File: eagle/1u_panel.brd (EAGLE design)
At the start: 83 x 100 mm, 65 parts, among them J1 1.27MM-SWD-CONNECTOR, U1 SPV1040, U5 P-CHANNELFET, U6 ON-N-CHANNEL-FET, U7 DIODE-INC-NPNSOT23HOLE

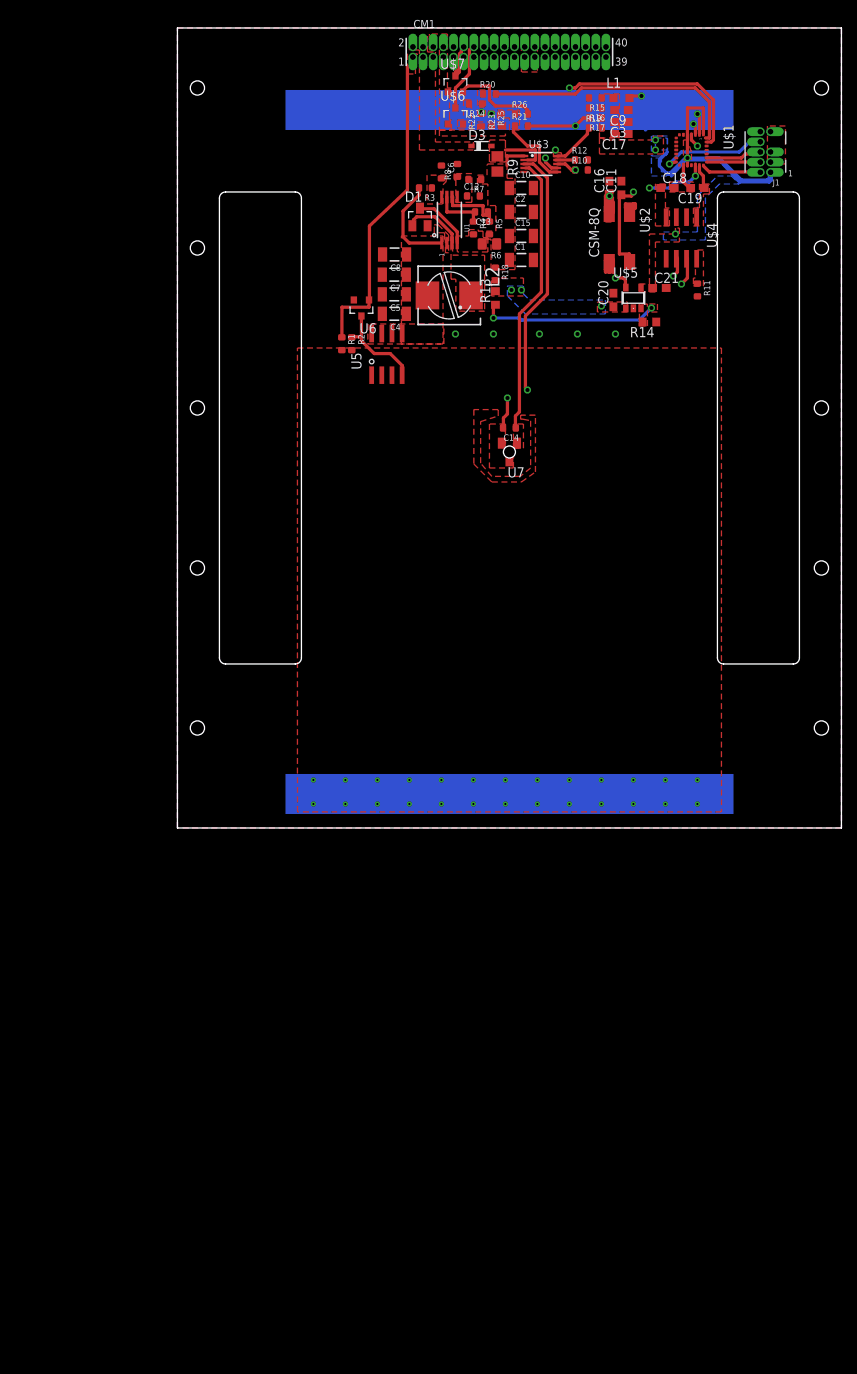
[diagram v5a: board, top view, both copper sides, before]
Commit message: OreSat rev0.5 structure changes with Calvin.
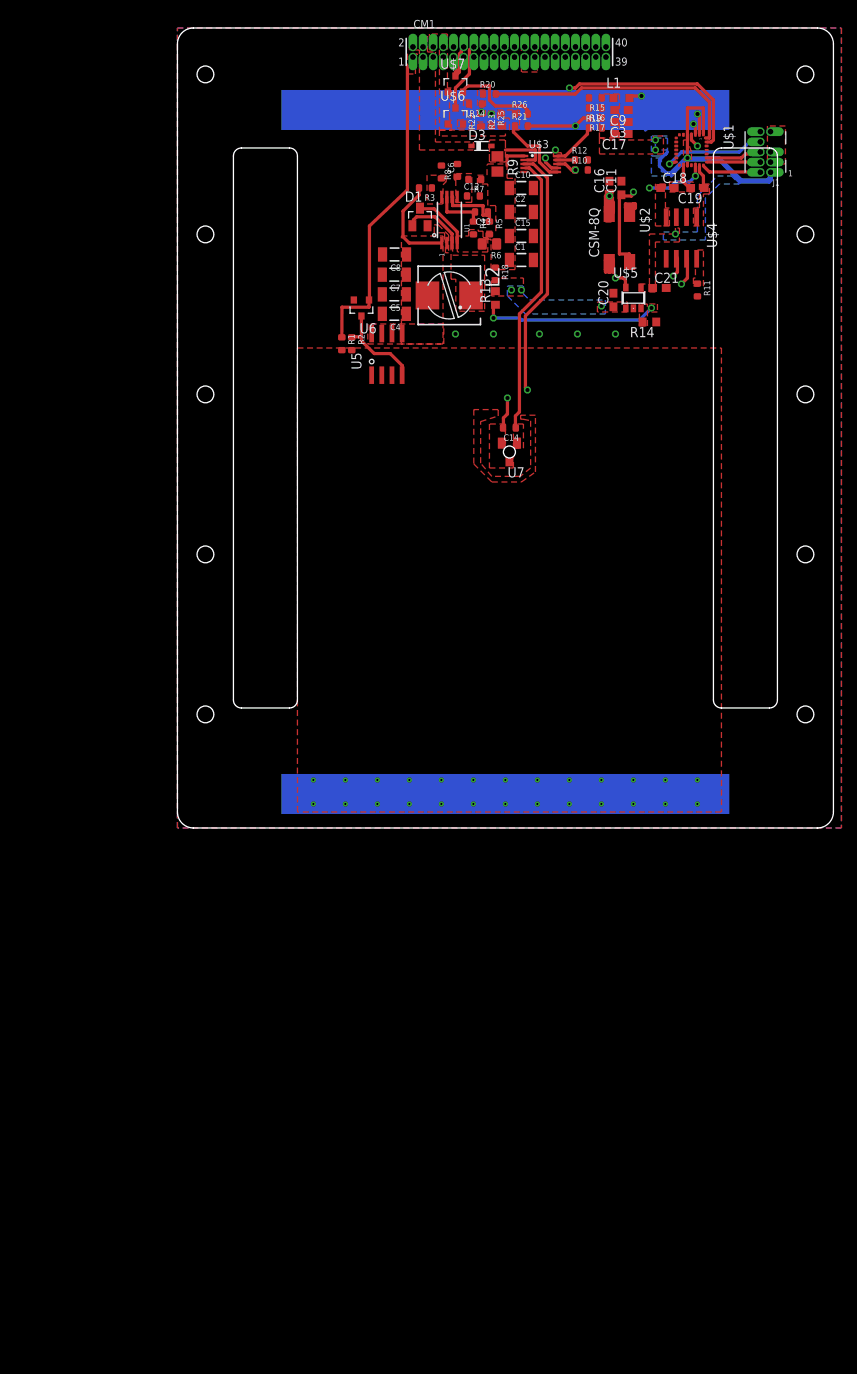
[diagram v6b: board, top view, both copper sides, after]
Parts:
- moved D2 0.50 mm to (41.0, 47.0)
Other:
- board size 83 x 100 mm -> 82 x 100 mm
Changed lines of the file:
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@@
 <?xml version="1.0" encoding="utf-8"?>
 <!DOCTYPE eagle SYSTEM "eagle.dtd">
-<eagle version="7.5.0">
+<eagle version="7.7.0">
 <drawing>
 <settings>
@@
 <layer number="23" name="tOrigins" color="15" fill="1" visible="yes" active="yes"/>
 <layer number="24" name="bOrigins" color="15" fill="1" visible="yes" active="yes"/>
-<layer number="25" name="tNames" color="7" fill="1" visible="yes" active="yes"/>
-<layer number="26" name="bNames" color="7" fill="1" visible="yes" active="yes"/>
-<layer number="27" name="tValues" color="7" fill="1" visible="yes" active="yes"/>
-<layer number="28" name="bValues" color="7" fill="1" visible="yes" active="yes"/>
+<layer number="25" name="tNames" color="7" fill="1" visible="no" active="yes"/>
+<layer number="26" name="bNames" color="7" fill="1" visible="no" active="yes"/>
+<layer number="27" name="tValues" color="7" fill="1" visible="no" active="yes"/>
+<layer number="28" name="bValues" color="7" fill="1" visible="no" active="yes"/>
 <layer number="29" name="tStop" color="7" fill="3" visible="yes" active="yes"/>
 <layer number="30" name="bStop" color="7" fill="6" visible="yes" active="yes"/>
-<layer number="31" name="tCream" color="7" fill="4" visible="yes" active="yes"/>
-<layer number="32" name="bCream" color="7" fill="5" visible="yes" active="yes"/>
-<layer number="33" name="tFinish" color="6" fill="3" visible="yes" active="yes"/>
-<layer number="34" name="bFinish" color="6" fill="6" visible="yes" active="yes"/>
-<layer number="35" name="tGlue" color="7" fill="4" visible="yes" active="yes"/>
-<layer number="36" name="bGlue" color="7" fill="5" visible="yes" active="yes"/>
-<layer number="37" name="tTest" color="7" fill="1" visible="yes" active="yes"/>
-<layer number="38" name="bTest" color="7" fill="1" visible="yes" active="yes"/>
-<layer number="39" name="tKeepout" color="4" fill="11" visible="yes" active="yes"/>
-<layer number="40" name="bKeepout" color="1" fill="11" visible="yes" active="yes"/>
-<layer number="41" name="tRestrict" color="4" fill="10" visible="yes" active="yes"/>
-<layer number="42" name="bRestrict" color="1" fill="10" visible="yes" active="yes"/>
-<layer number="43" name="vRestrict" color="2" fill="10" visible="yes" active="yes"/>
-<layer number="44" name="Drills" color="7" fill="1" visible="yes" active="yes"/>
-<layer number="45" name="Holes" color="7" fill="1" visible="yes" active="yes"/>
+<layer number="31" name="tCream" color="7" fill="4" visible="no" active="yes"/>
+<layer number="32" name="bCream" color="7" fill="5" visible="no" active="yes"/>
+<layer number="33" name="tFinish" color="6" fill="3" visible="no" active="yes"/>
+<layer number="34" name="bFinish" color="6" fill="6" visible="no" active="yes"/>
+<layer number="35" name="tGlue" color="7" fill="4" visible="no" active="yes"/>
+<layer number="36" name="bGlue" color="7" fill="5" visible="no" active="yes"/>
+<layer number="37" name="tTest" color="7" fill="1" visible="no" active="yes"/>
+<layer number="38" name="bTest" color="7" fill="1" visible="no" active="yes"/>
+<layer number="39" name="tKeepout" color="4" fill="11" visible="no" active="yes"/>
+<layer number="40" name="bKeepout" color="1" fill="11" visible="no" active="yes"/>
+<layer number="41" name="tRestrict" color="4" fill="10" visible="no" active="yes"/>
+<layer number="42" name="bRestrict" color="1" fill="10" visible="no" active="yes"/>
+<layer number="43" name="vRestrict" color="2" fill="10" visible="no" active="yes"/>
+<layer number="44" name="Drills" color="7" fill="1" visible="no" active="yes"/>
+<layer number="45" name="Holes" color="7" fill="1" visible="no" active="yes"/>
 <layer number="46" name="Milling" color="3" fill="1" visible="yes" active="yes"/>
-<layer number="47" name="Measures" color="7" fill="1" visible="yes" active="yes"/>
+<layer number="47" name="Measures" color="7" fill="1" visible="no" active="yes"/>
 <layer number="48" name="Document" color="7" fill="1" visible="yes" active="yes"/>
-<layer number="49" name="Reference" color="7" fill="1" visible="yes" active="yes"/>
+<layer number="49" name="Reference" color="7" fill="1" visible="no" active="yes"/>
 <layer number="51" name="tDocu" color="7" fill="1" visible="yes" active="yes"/>
 <layer number="52" name="bDocu" color="7" fill="1" visible="yes" active="yes"/>
@@
 <board>
 <plain>
-<wire x1="0" y1="0" x2="83" y2="0" width="0" layer="20"/>
-<wire x1="83" y1="0" x2="83" y2="100" width="0" layer="20"/>
-<wire x1="83" y1="100" x2="0" y2="100" width="0" layer="20"/>
-<wire x1="0" y1="100" x2="0" y2="0" width="0" layer="20"/>
-<hole x="2.5" y="12.5" drill="1.78"/>
-<hole x="2.5" y="32.5" drill="1.78"/>
-<hole x="2.5" y="52.5" drill="1.78"/>
-<hole x="2.5" y="72.5" drill="1.78"/>
-<hole x="2.5" y="92.5" drill="1.78"/>
-<hole x="80.5" y="12.5" drill="1.78"/>
-<hole x="80.5" y="32.5" drill="1.78"/>
-<hole x="80.5" y="52.5" drill="1.78"/>
-<hole x="80.5" y="72.5" drill="1.78"/>
-<hole x="80.5" y="92.5" drill="1.78"/>
-<wire x1="14.732" y1="20.5" x2="6.018" y2="20.5" width="0.1" layer="20"/>
-<wire x1="6.018" y1="20.5" x2="5.25" y2="21.268" width="0.1" layer="20" curve="-90"/>
-<wire x1="5.25" y1="21.268" x2="5.25" y2="78.732" width="0.1" layer="20"/>
-<wire x1="5.25" y1="78.732" x2="6.018" y2="79.5" width="0.1" layer="20" curve="-90"/>
-<wire x1="6.018" y1="79.5" x2="14.732" y2="79.5" width="0.1" layer="20"/>
-<wire x1="14.732" y1="79.5" x2="15.5" y2="78.732" width="0.1" layer="20" curve="-90"/>
-<wire x1="15.5" y1="78.732" x2="15.5" y2="21.268" width="0.1" layer="20"/>
-<wire x1="15.5" y1="21.268" x2="14.732" y2="20.5" width="0.1" layer="20" curve="-90"/>
-<wire x1="68.268" y1="20.5" x2="76.982" y2="20.5" width="0.1" layer="20"/>
-<wire x1="76.982" y1="20.5" x2="77.75" y2="21.268" width="0.1" layer="20" curve="90"/>
-<wire x1="77.75" y1="21.268" x2="77.75" y2="78.732" width="0.1" layer="20"/>
-<wire x1="77.75" y1="78.732" x2="76.982" y2="79.5" width="0.1" layer="20" curve="90"/>
-<wire x1="76.982" y1="79.5" x2="68.268" y2="79.5" width="0.1" layer="20"/>
-<wire x1="68.268" y1="79.5" x2="67.5" y2="78.732" width="0.1" layer="20" curve="90"/>
-<wire x1="67.5" y1="78.732" x2="67.5" y2="21.268" width="0.1" layer="20"/>
-<wire x1="67.5" y1="21.268" x2="68.268" y2="20.5" width="0.1" layer="20" curve="90"/>
+<wire x1="80" y1="100" x2="2" y2="100" width="0" layer="20"/>
+<wire x1="2" y1="100" x2="0" y2="98" width="0" layer="20" curve="90"/>
+<wire x1="0" y1="98" x2="0" y2="2" width="0" layer="20"/>
+<wire x1="0" y1="2" x2="2" y2="0" width="0" layer="20" curve="90"/>
+<wire x1="2" y1="0" x2="80" y2="0" width="0" layer="20"/>
+<wire x1="80" y1="0" x2="82" y2="2" width="0" layer="20" curve="90"/>
+<wire x1="82" y1="2" x2="82" y2="98" width="0" layer="20"/>
+<wire x1="82" y1="98" x2="80" y2="100" width="0" layer="20" curve="90"/>
+<hole x="3.5" y="14.2" drill="2.1"/>
+<hole x="3.5" y="34.2" drill="2.1"/>
+<hole x="3.5" y="54.2" drill="2.1"/>
+<hole x="3.5" y="74.2" drill="2.1"/>
+<hole x="3.5" y="94.2" drill="2.1"/>
+<hole x="78.5" y="14.2" drill="2.1"/>
+<hole x="78.5" y="34.2" drill="2.1"/>
+<hole x="78.5" y="54.2" drill="2.1"/>
+<hole x="78.5" y="74.2" drill="2.1"/>
+<hole x="78.5" y="94.2" drill="2.1"/>
+<wire x1="15" y1="84" x2="15" y2="16" width="0.1" layer="20"/>
+<wire x1="15" y1="16" x2="14" y2="15" width="0.1" layer="20" curve="-90"/>
+<wire x1="14" y1="15" x2="8" y2="15" width="0.1" layer="20"/>
+<wire x1="8" y1="15" x2="7" y2="16" width="0.1" layer="20" curve="-90"/>
+<wire x1="7" y1="16" x2="7" y2="84" width="0.1" layer="20"/>
+<wire x1="7" y1="84" x2="8" y2="85" width="0.1" layer="20" curve="-90"/>
+<wire x1="8" y1="85" x2="14" y2="85" width="0.1" layer="20"/>
+<wire x1="14" y1="85" x2="15" y2="84" width="0.1" layer="20" curve="-90"/>
+<wire x1="67" y1="16" x2="67" y2="84" width="0.1" layer="20"/>
+<wire x1="67" y1="84" x2="68" y2="85" width="0.1" layer="20" curve="-90"/>
+<wire x1="68" y1="85" x2="74" y2="85" width="0.1" layer="20"/>
+<wire x1="67" y1="16" x2="68" y2="15" width="0.1" layer="20" curve="90"/>
+<wire x1="68" y1="15" x2="74" y2="15" width="0.1" layer="20"/>
+<wire x1="74" y1="15" x2="75" y2="16" width="0.1" layer="20" curve="90"/>
+<wire x1="74" y1="85" x2="75" y2="84" width="0.1" layer="20" curve="-90"/>
+<wire x1="75" y1="84" x2="75" y2="16" width="0.1" layer="20"/>
 </plain>
 <attributes>
@@
 <element name="R9" library="rcl" package="R0805" value="" x="40" y="83" rot="R270"/>
 <element name="C14" library="rcl_custom" package=".0603-B-NOSILK" value="20u" x="41.5" y="50" rot="R180"/>
-<element name="D2" library="alta-cell" package="ALTA-FIVE-CELL" value="ALTA-5-CELL-ARRAY" x="41.5" y="47" locked="yes" rot="MR0"/>
+<element name="D2" library="alta-cell" package="ALTA-FIVE-CELL" value="ALTA-5-CELL-ARRAY" x="41" y="47" locked="yes" rot="MR0"/>
 <element name="U1" library="spv1040" package="TSSOP-8" value="SPV1040" x="34" y="76" rot="R90"/>
 <element name="U$3" library="LTC2990" package="MSOP10" value="LTC2990" x="45.41" y="83" rot="R270"/>
@@
 <contactref element="R2" pad="2"/>
 <contactref element="U5" pad="2"/>
-<wire x1="41.5" y1="4.25" x2="42.8" y2="4.25" width="0.2" layer="16"/>
+<wire x1="41" y1="4.25" x2="42.8" y2="4.25" width="0.2" layer="16"/>
 <via x="17" y="6" extent="1-16" drill="0.254"/>
 <via x="17" y="3" extent="1-16" drill="0.254"/>
@@
 <via x="45" y="6" extent="1-16" drill="0.254"/>
 <via x="45" y="3" extent="1-16" drill="0.254"/>
-<wire x1="41.5" y1="4.25" x2="41" y2="4.25" width="0.2" layer="16"/>
 <wire x1="41" y1="4.25" x2="41" y2="3" width="0.2" layer="16"/>
 <via x="49" y="6" extent="1-16" drill="0.254"/>

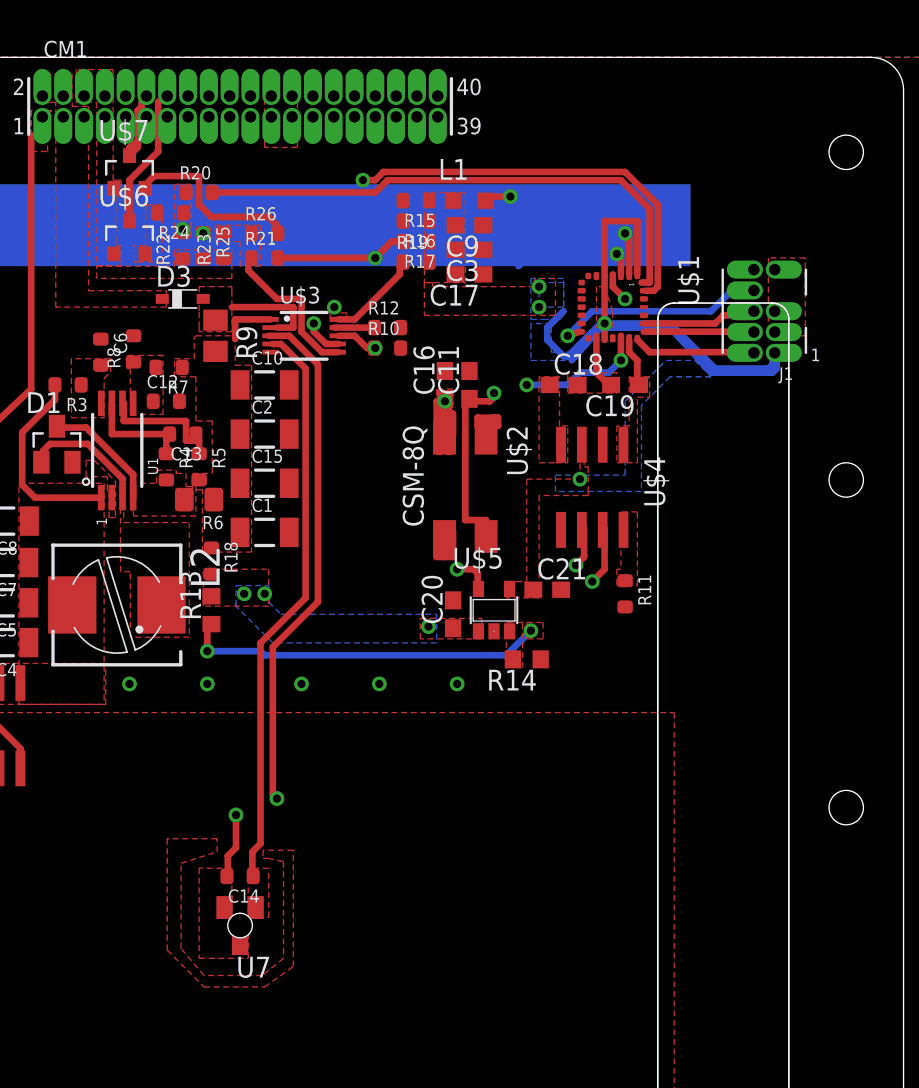
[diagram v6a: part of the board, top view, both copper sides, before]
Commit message: We deciderated: STM for the win. We're dorks.
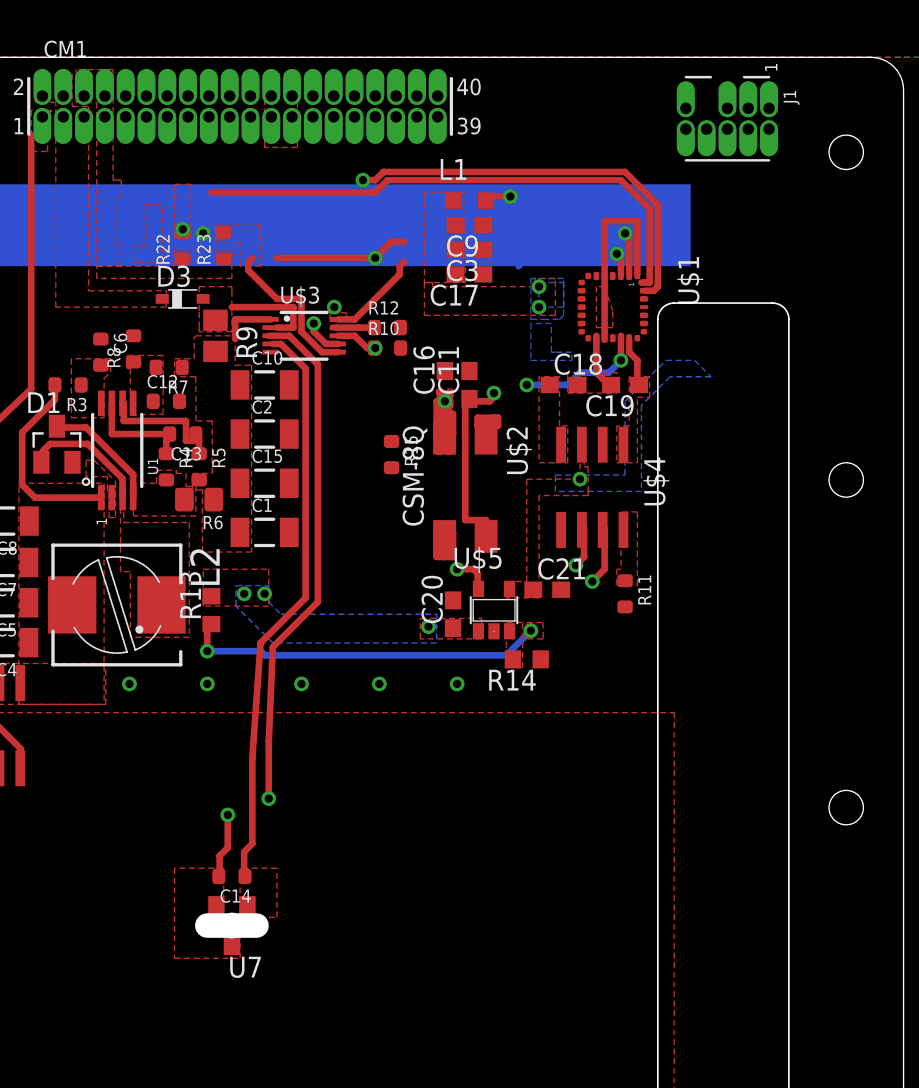
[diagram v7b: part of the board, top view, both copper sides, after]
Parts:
- removed R16, R17: 5.6k, rcl_custom:.0603-B-NOSILK
- removed R18, R19, R20, R21, R24, R25, R26: NP, rcl_custom:.0603-B-NOSILK
- removed U$6, U$7: ON-N-CHANNEL-FET, on-n-channel-fet:SOT23
- L2: value (none) -> 47u
- R22, R23: value NP -> 4.7k
- moved R15 15.6 mm to (50.8, 75.8), turned to 270 degrees
- moved J1 12.0 mm to (71.2, 96.2), turned to 270 degrees
- moved C14 0.50 mm to (41.0, 50.0)
- moved U7 0.50 mm to (41.0, 47.0)
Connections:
- removed net N$3: R15.2, R16.2
- removed net SCLOPT1ON: R24.2, U$6.2
- removed net SCLOPT1OUT: CM1.P$14, U$6.3
- removed net SDAOPT1: R21.1, R23.2, R26.1, U$3.6
- removed net SDAOPT1ON: R26.2, U$7.2
- removed net SDAOPT1OUT: CM1.P$12, U$7.3
- removed net SDAOPT2: R20.2, U$1.28
- removed net SOLAR-IN-SWITCHED1: C1.1, C10.1, C15.1, C2.1, R18.1, R5.2, R6.1, R7.1, R9.2, U$3.1
- removed net VCCOPT1: R19.1, R25.1, U$3.10
- removed net VCCOPT2: CM1.P$6, CM1.P$7, CM1.P$8, R22.1, R23.1, R25.2, U$6.1, U$7.1
- net 3.3V: now also R15.2, R22.1, R23.1, U$3.10; no longer R15.1, R16.1, R17.1, R19.2
- net ADDRSELECT: no longer CM1.P$15, CM1.P$16
- net CANH: now also CM1.P$7, CM1.P$8; no longer CM1.P$17
- net CANL: now also CM1.P$10, CM1.P$9; no longer CM1.P$19
- net GND: now also CM1.P$1, CM1.P$2; no longer CM1.P$23, CM1.P$24, CM1.P$25, CM1.P$26
- net RESET: now also R15.1
- net SCLOPT1: now also U$1.28; no longer R20.1, R24.1
- net SCLOPT2: now also R23.2, U$3.6; no longer R17.2, R21.2
- net SHORT: now also CM1.P$5, CM1.P$6; no longer CM1.P$1
- net SOLAR-IN-SWITCHED2: now also C1.1, C10.1, C15.1, C2.1, R5.2, R6.1, R7.1, R9.2, U$3.1; no longer R18.2
- net SWITCHEDOUT: no longer CM1.P$2, CM1.P$5
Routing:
- net N$2: track 0.00 -> 35.0 mm
- net N$1: track 0.00 -> 35.0 mm
- net 3.3V: track 47.4 -> 12.5 mm, vias 4 -> 3
- net TDI: track 13.2 -> 0.00 mm, vias 1 -> 0
- net SDAOPT1ON: track 11.1 -> 0.00 mm
- net RESET: track 10.3 -> 0.00 mm, vias 1 -> 0
- net SCLOPT1OUT: track 8.68 -> 0.00 mm
- net SWDIO: track 7.31 -> 0.00 mm
- net SWO: track 6.81 -> 0.00 mm
- net SWDCLK: track 6.50 -> 0.00 mm
- net SDAOPT1OUT: track 4.77 -> 0.00 mm
- net SOLAR-IN-SWITCHED2: track 0.00 -> 3.36 mm
- net SOLAR-IN-SWITCHED1: track 3.36 -> 0.00 mm
- removed copper zone on layer 15, net N$2
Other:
- outline, holes or cut-outs redrawn
